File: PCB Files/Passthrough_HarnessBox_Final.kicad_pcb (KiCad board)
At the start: 4 copper layers, 73 x 43 mm, 25 parts, among them J1 JAE DX07S024XJ1R1100, J2 Molex 2125280400, J3 JAE MX34032NF4, J4 JAE MX34032NF4, J5 1790513, J6 Conn_01x03_Pin, K1 TQ2-12V, Q1 DMN3200U-7, U1 Vishay DG419LEDY-T1-GE4, U2 Vishay DG419LEDY-T1-GE4

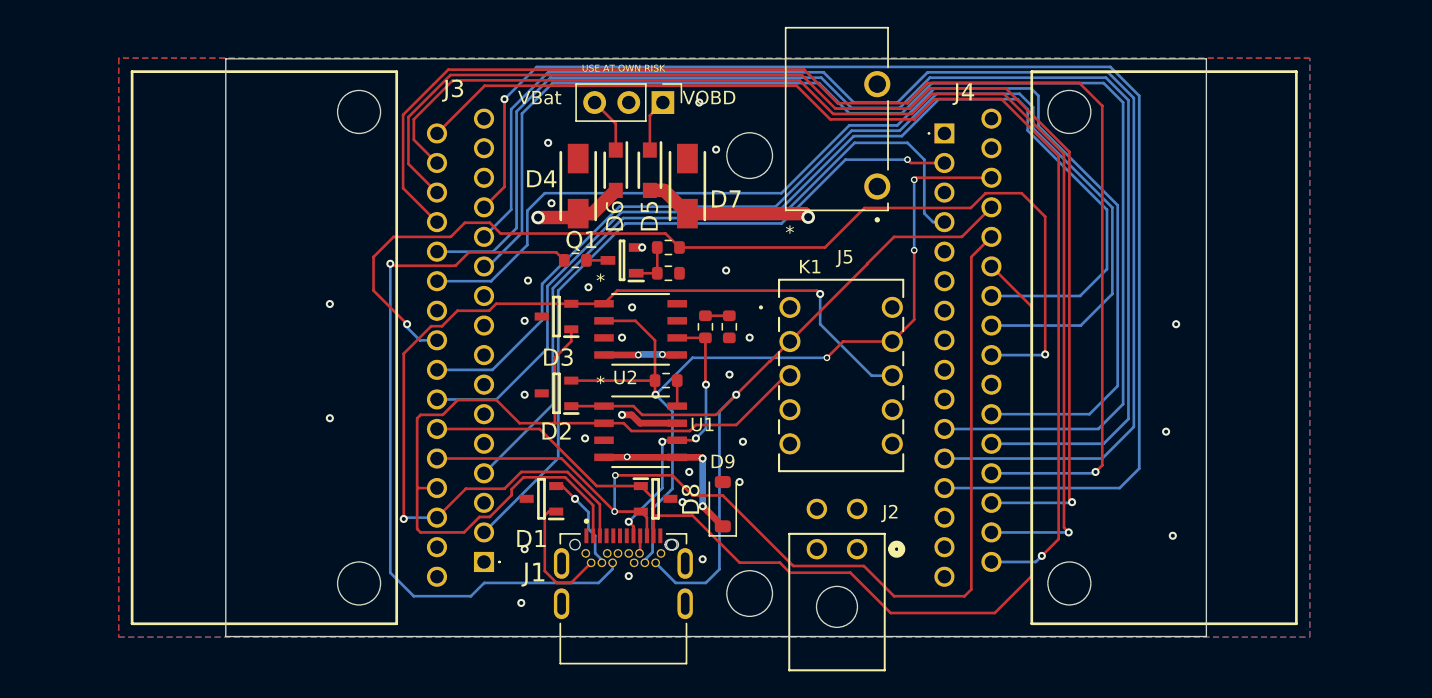
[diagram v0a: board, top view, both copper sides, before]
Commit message: Update to _Final KiCad revision
Replaces the schematic/PCB/project files with the newer
Passthrough_HarnessBox_Final revision from active design work
(~7 weeks of further changes). Drops the now-stale .kicad_dru/.kicad_prl
(not present in the Final project) and notes in the README that the
existing design review/analysis predate this revision.
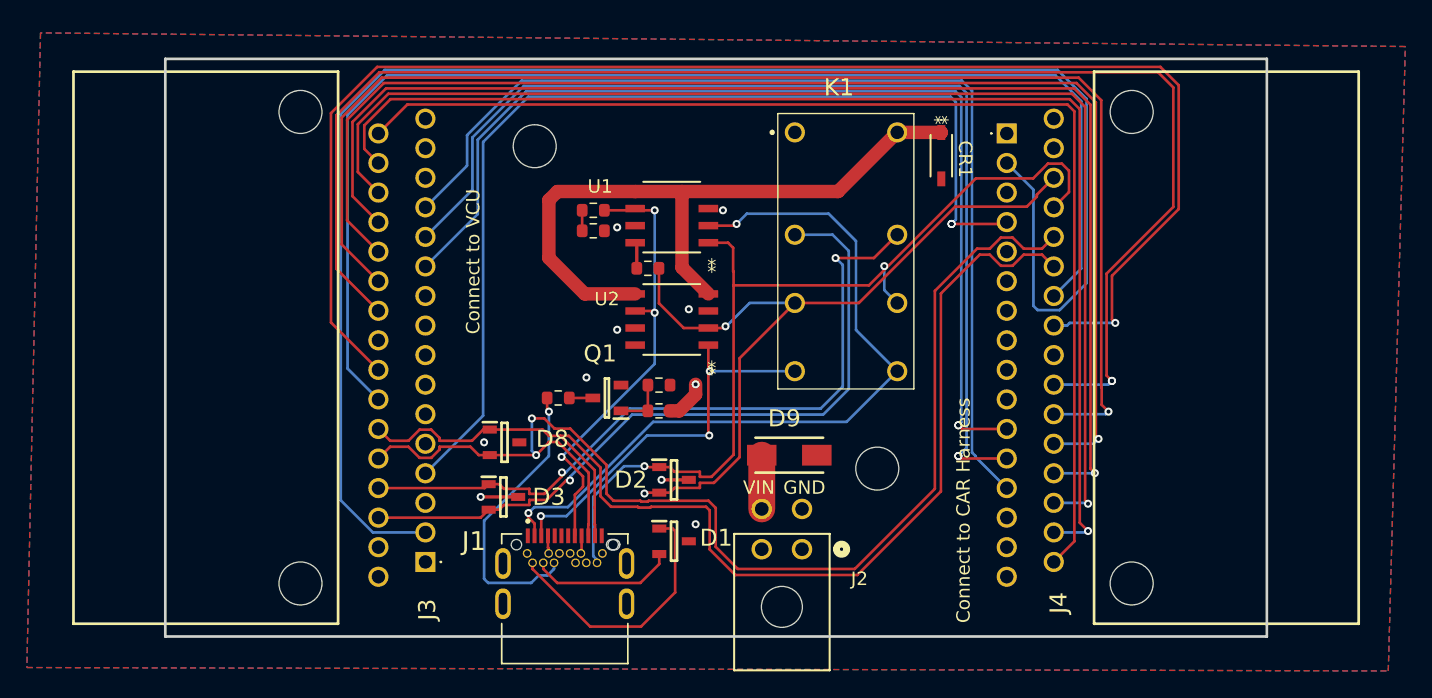
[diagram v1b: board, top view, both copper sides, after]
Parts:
- removed D4, D7: 16V, * My_Components:SMAJ16A
- removed D5, D6: STPS2H100ZFY, * My_Components:STPS2H100ZFY
- removed J5: 1790513, footprints:PHOENIX_1790513
- removed J6: Conn_01x03_Pin, Connector_PinHeader_2.54mm:PinHeader_1x03_P2.54mm_Vertical
- added CR1: 1N4148W-7-F, Footprints:SOD123_DIO, F.Cu at (159.8, 76.7)
- D1, D2, D3, D8: footprint * My_Components:PESD1CAN -> My_Components:PESD1CAN
- D9: value 1N4148W -> 16V; footprint Diode_SMD:D_SOD-123 -> My_Components:SMAJ16A
- J1: footprint * My_Components:JAE DX07S024XJ1R1100 -> My_Components:JAE DX07S024XJ1R1100
- J2: footprint * My_Components:Molex 2125280400 -> My_Components:Molex 2125280400
- J3, J4: footprint * My_Components:JAE MX34032NF4 -> My_Components:JAE MX34032NF4
- K1: value TQ2-12V -> G5V-2 DC12; footprint footprints:RELAY_TQ2_PAN -> My_Components:Omron G5V-2-DC12
- Q1: footprint * My_Components:DMN3200U-7 -> My_Components:DMN3200U-7
- R2, R3, R4: footprint * My_Components:Rohm ESR03EZPJ121 -> My_Components:Rohm ESR03EZPJ121
- R6, R7, R8: footprint * My_Components:Rohm ESR03EZPJ102 -> My_Components:Rohm ESR03EZPJ102
- U1, U2: footprint * My_Components:Vishay DG419LEDY-T1-GE4 -> My_Components:Vishay DG419LEDY-T1-GE4
- moved U1 16.1 mm to (139.7, 81.3), turned to 180 degrees
- moved D3 14.0 mm to (127.2, 102.1), turned to 0 degrees
- moved R3 12.4 mm to (133.9, 82.3), turned to 0 degrees
- moved R6 12.2 mm to (138.7, 95.7)
- moved R2 12.0 mm to (133.9, 80.8), turned to 180 degrees
- moved D8 12.0 mm to (127.3, 98.0)
- moved D2 10.9 mm to (139.9, 100.8), turned to 0 degrees
- moved D1 10.4 mm to (139.9, 105.4), turned to 0 degrees
- moved R7 10.3 mm to (131.2, 94.7)
- moved Q1 10.3 mm to (134.9, 94.7)
- moved R4 8.46 mm to (137.9, 85.1), turned to 0 degrees
- moved R8 8.35 mm to (138.7, 93.8)
- moved D9 6.15 mm to (148.4, 99.0), turned to 0 degrees
- moved K1 5.72 mm to (152.4, 83.8), turned to -90 degrees
- moved J4 4.64 mm to (164.6, 75.0)
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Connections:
- net /COMMA_H renamed /COMMA_P
- net /COMMA_L renamed /COMMA_N
- net /RADAR_H renamed /RADAR_P
- net /RADAR_L renamed /RADAR_N
- net /VBAT renamed /Harness_12v
- net Net-(J3-Pad13) renamed /Harness_GND
- D2 pad 1: /CAMERA_H -> /CAMERA_P
- D2 pad 2: /CAMERA_L -> /CAMERA_N
- D3 pad 1: /VCU_H -> /VCU_P
- D3 pad 2: /VCU_L -> /VCU_N
- J1 pad A2: /VCU_H -> /VCU_P_C
- J1 pad A3: /VCU_L -> /VCU_N_C
- J1 pad A4: GND -> VIN
- J1 pad B2: /CAMERA_H -> /CAMERA_P
- J1 pad B3: /CAMERA_L -> /CAMERA_N
- J2 pad 4: VOBD -> VIN
- J3 pad 19: /VCU_L -> /VCU_N
- J3 pad 20: /VCU_H -> /VCU_P
- J4 pad 19: /CAMERA_L -> /CAMERA_N
- J4 pad 20: /CAMERA_H -> /CAMERA_P
- K1 pad 1: VIN -> GND
- K1 pad 4: unconnected-(K1-Pad4) -> /VCU_N
- K1 pad 6: unconnected-(K1-Pad6) -> /CAMERA_N
- K1 pad 8: /VCU_L -> /VCU_N_C
- K1 pad 9: /CAMERA_L -> /VCU_P_C
- R4 pad 2: /CAMERA_L -> /CAMERA_N
- U1 pad 1: /CAMERA_H -> /CAMERA_P
- U1 pad 2: /VCU_H -> /VCU_P_C
- U2 pad 1: /VCU_L -> /VCU_N_C
- U2 pad 2: /CAMERA_L -> /CAMERA_N
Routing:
- net /IGN: track 77.4 -> 175.9 mm, vias 2 -> 1
- net /VCU_L: track 74.4 -> 0.00 mm, vias 2 -> 0
- net Net-(J3-Pad2): track 53.2 -> 123.9 mm, vias 1 -> 0
- net /CAMERA_P: track 0.00 -> 70.4 mm, vias 0 -> 2
- net /CAMERA_N: track 0.00 -> 67.7 mm, vias 0 -> 2
- net /VCU_H: track 66.5 -> 0.00 mm
- net /CAMERA_L: track 66.4 -> 0.00 mm, vias 4 -> 0
- net /CAMERA_H: track 57.3 -> 0.00 mm, vias 1 -> 0
- net /VCU_P_C: track 0.00 -> 56.9 mm, vias 0 -> 2
- net /VCU_N: track 0.00 -> 54.2 mm, vias 0 -> 1
- net /VCU_P: track 0.00 -> 53.8 mm, vias 0 -> 2
- net VIN: track 70.8 -> 116.4 mm, vias 5 -> 0
- net VOBD: track 36.2 -> 0.00 mm, vias 1 -> 0
- net /SBU 2: track 55.3 -> 21.7 mm
- net Net-(J3-Pad24): track 81.2 -> 111.1 mm, vias 0 -> 1
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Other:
- board size 73 x 43 mm -> 82 x 43 mm
- board text added: "12v"
- board text added: "Connect to CAR Harness"
- board text added: "Connect to VCU"
- board text added: "GND"
- board text added: "VIN"
- board text removed: "USE AT OWN RISK"
- board text removed: "VBat"
- board text removed: "VOBD"
